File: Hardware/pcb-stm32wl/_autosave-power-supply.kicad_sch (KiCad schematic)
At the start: 40 parts, among them J2 JST-PH, Q1 PMV32UP,215, U1 TPS22917DBV, U11 MIC5365-3.3YD5, U12 TPS22917DBV, U2 TPS3839G18DBZT‎, U4 RP605Z283B, U8 MAX1837ETT50+T, U9 WE-TPC_5828

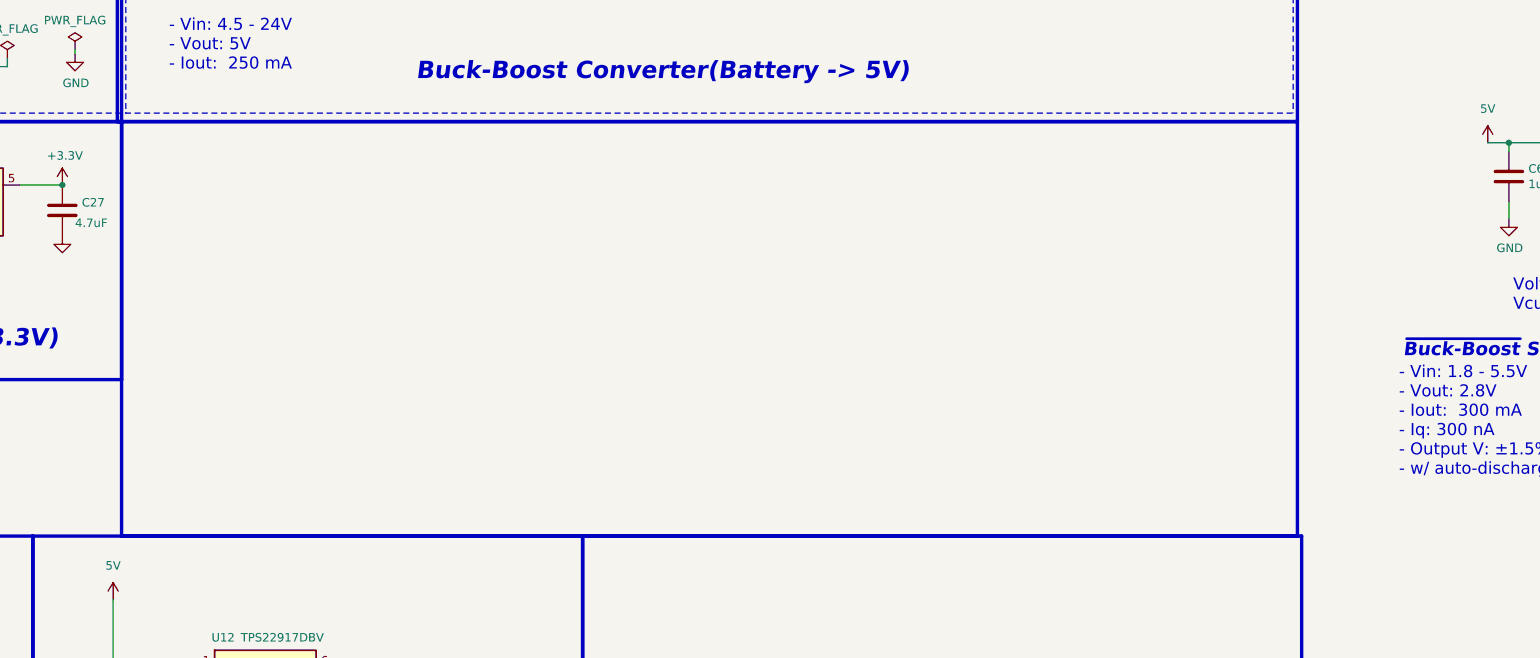
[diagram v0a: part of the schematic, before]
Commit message: power circuitry completely wired
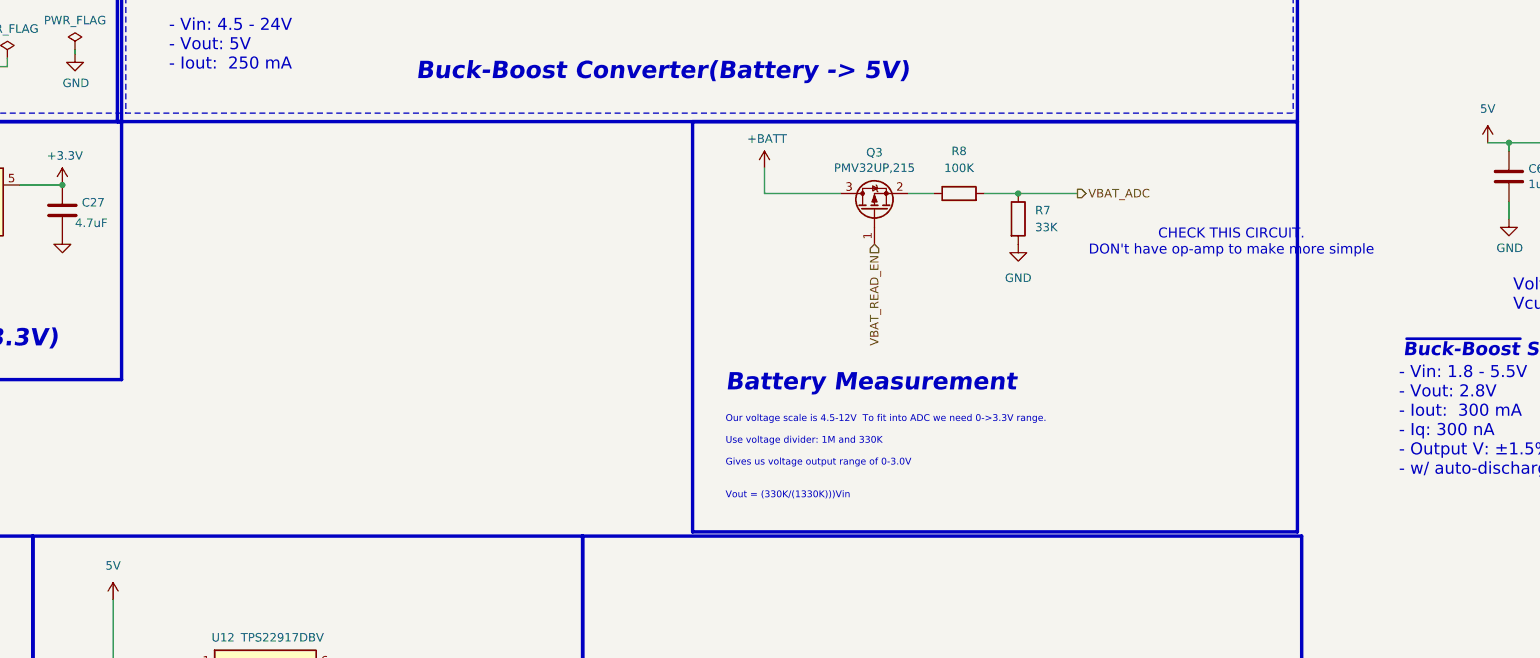
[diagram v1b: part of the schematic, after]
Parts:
- added Q3: PMV32UP,215, Package_TO_SOT_SMD:SOT-23, symbol Device:Q_PMOS_GSD
- added R7: 33K, symbol Device:R
- added R8: 100K, symbol Device:R
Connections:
- net +3.3V: now also Q3.3 (D)
- net GND: now also R7.2
- net VBAT_ADC: now also R7.1, R8.2
- net VBAT_READ_EN: now also Q3.1 (G)
- new net: Q3.2 (S), R8.1
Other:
- note added: "Battery Measurement"
- note added: "CHECK THIS CIRCUIT. DON't have op-amp to make more simple"
- note added: "Our voltage scale is 4.5-12V To fit into ADC we need 0->3.3V range. Use voltage divider: 1M and 330K Gives us voltage output range of 0-3.0V Vout = (330K/(1330K)))Vin"
